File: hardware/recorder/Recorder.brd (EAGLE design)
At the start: 66.5 x 73.7 mm, 23 parts, among them U1 PDM1-S5-D12-S, U2 LM6132BIN, U3 Value, U4 L7908CV, U5 L7808ABV, U6 ZVN4424A, U7 TEENSY_3.6_DIL

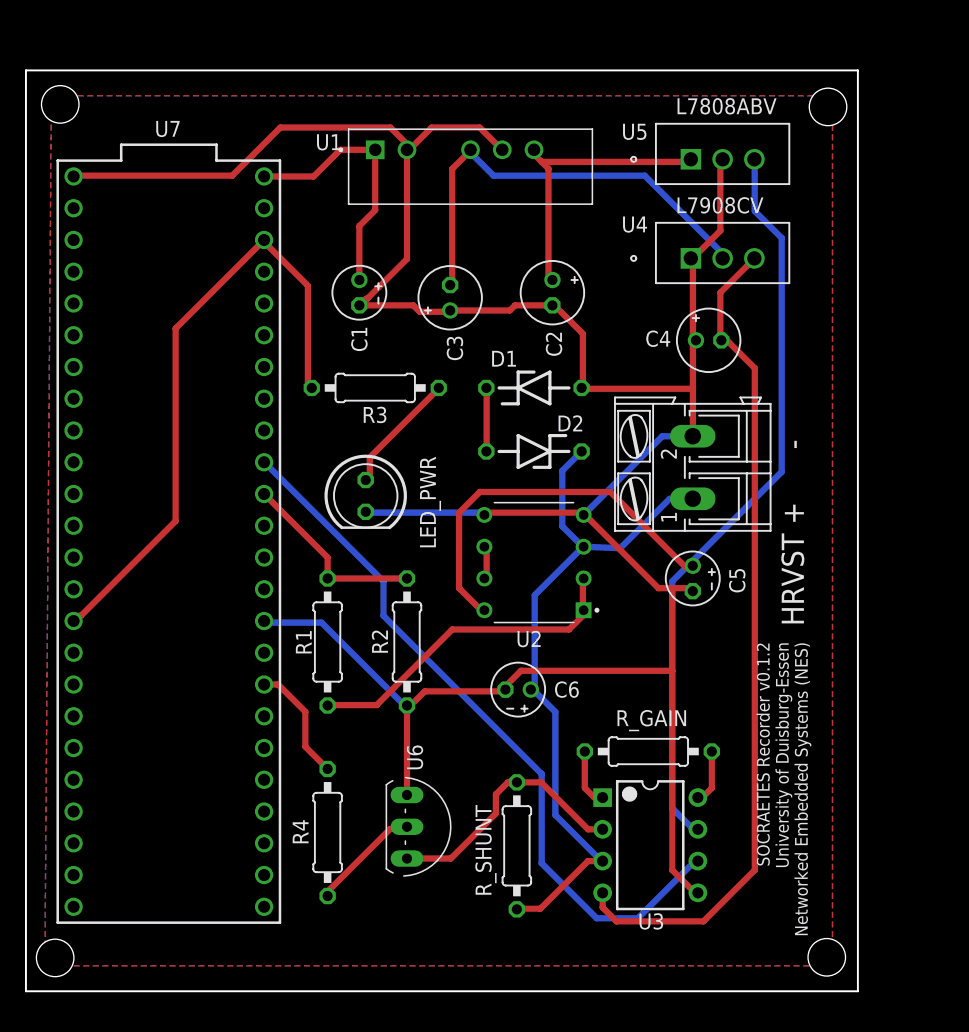
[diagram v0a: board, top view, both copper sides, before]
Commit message: Add vias, fix ground pour on the top layer
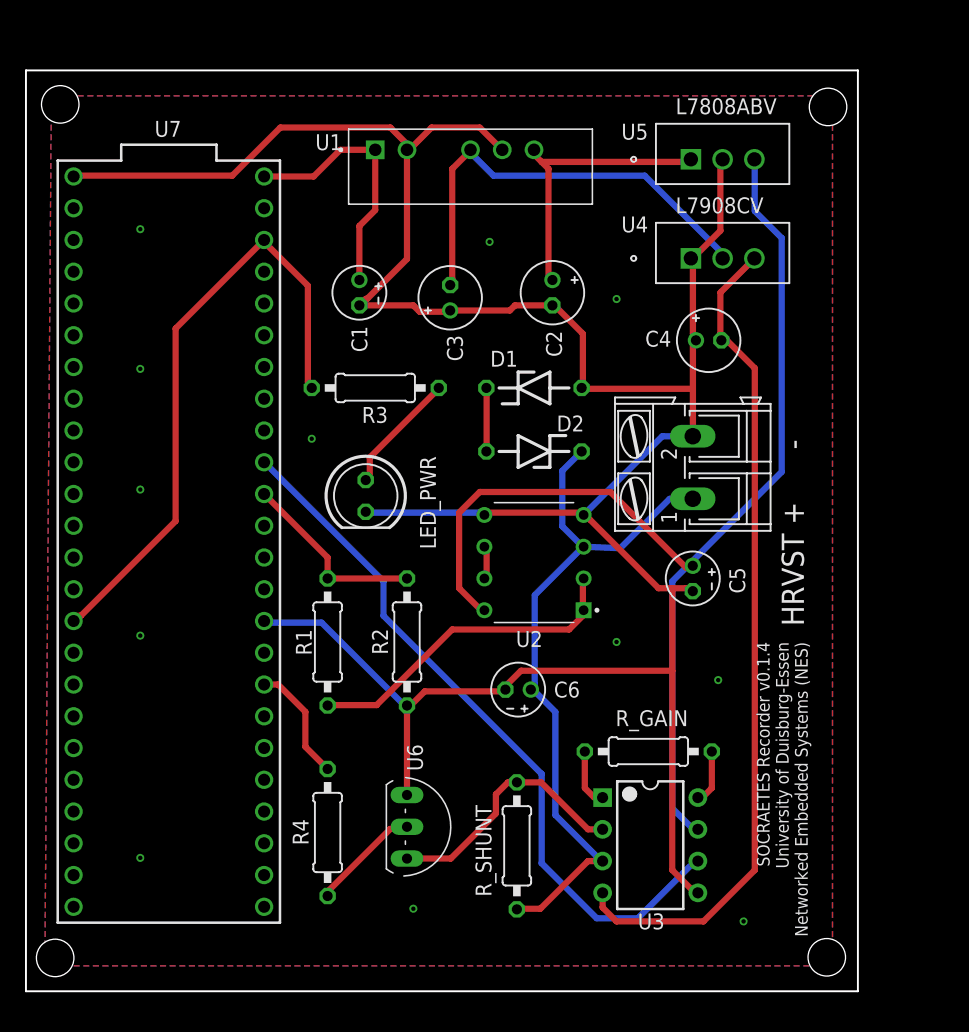
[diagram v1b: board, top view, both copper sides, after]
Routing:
- net GND: vias 0 -> 12
- added copper zone on layer 1, net GND
- removed copper zone on layer 1, net GND1
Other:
- board text added: "SOCRAETES Recorder v0.1.4 University of Duisburg-Essen Networked Embedded Systems (NES)"
- board text removed: "SOCRAETES Recorder v0.1.2 University of Duisburg-Essen Networked Embedded Systems (NES)"
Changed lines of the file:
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@@
 <plain>
 <text x="62.23" y="29.21" size="1.778" layer="25" rot="R90">HRVST +      -</text>
-<text x="58.4708" y="27.94" size="1.016" layer="25" rot="R270">SOCRAETES Recorder v0.1.2
+<text x="58.4708" y="27.94" size="1.016" layer="25" rot="R270">SOCRAETES Recorder v0.1.4
 University of Duisburg-Essen
 Networked Embedded Systems (NES)</text>
@@
 <vertex x="2.032" y="71.628"/>
 </polygon>
+<polygon width="0.5" layer="1" isolate="0.254">
+<vertex x="1.512628125" y="2.032"/>
+<vertex x="64.516" y="2.032"/>
+<vertex x="64.516" y="71.628"/>
+<vertex x="2.032" y="71.628"/>
+</polygon>
+<via x="55.372" y="24.892" extent="1-16" drill="0.35"/>
+<via x="9.144" y="60.96" extent="1-16" drill="0.35"/>
+<via x="9.144" y="49.784" extent="1-16" drill="0.35"/>
+<via x="9.144" y="40.132" extent="1-16" drill="0.35"/>
+<via x="9.144" y="28.448" extent="1-16" drill="0.35"/>
+<via x="9.144" y="10.668" extent="1-16" drill="0.35"/>
+<via x="30.988" y="6.604" extent="1-16" drill="0.35"/>
+<via x="47.244" y="27.94" extent="1-16" drill="0.35"/>
+<via x="57.404" y="5.588" extent="1-16" drill="0.35"/>
+<via x="47.244" y="55.372" extent="1-16" drill="0.35"/>
+<via x="37.084" y="59.944" extent="1-16" drill="0.35"/>
+<via x="22.86" y="44.196" extent="1-16" drill="0.35"/>
 </signal>
 <signal name="+12V">
@@
 <wire x1="30.25" y1="12.99" x2="30.48" y2="13.1572" width="0.5" layer="1"/>
 </signal>
-<signal name="GND1">
-<polygon width="0.5" layer="1" isolate="0.254">
-<vertex x="1.512628125" y="2.032"/>
-<vertex x="64.516" y="2.032"/>
-<vertex x="64.516" y="71.628"/>
-<vertex x="2.032" y="71.628"/>
-</polygon>
-</signal>
 </signals>

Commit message: Migrate recorder board to Teensy 4.1
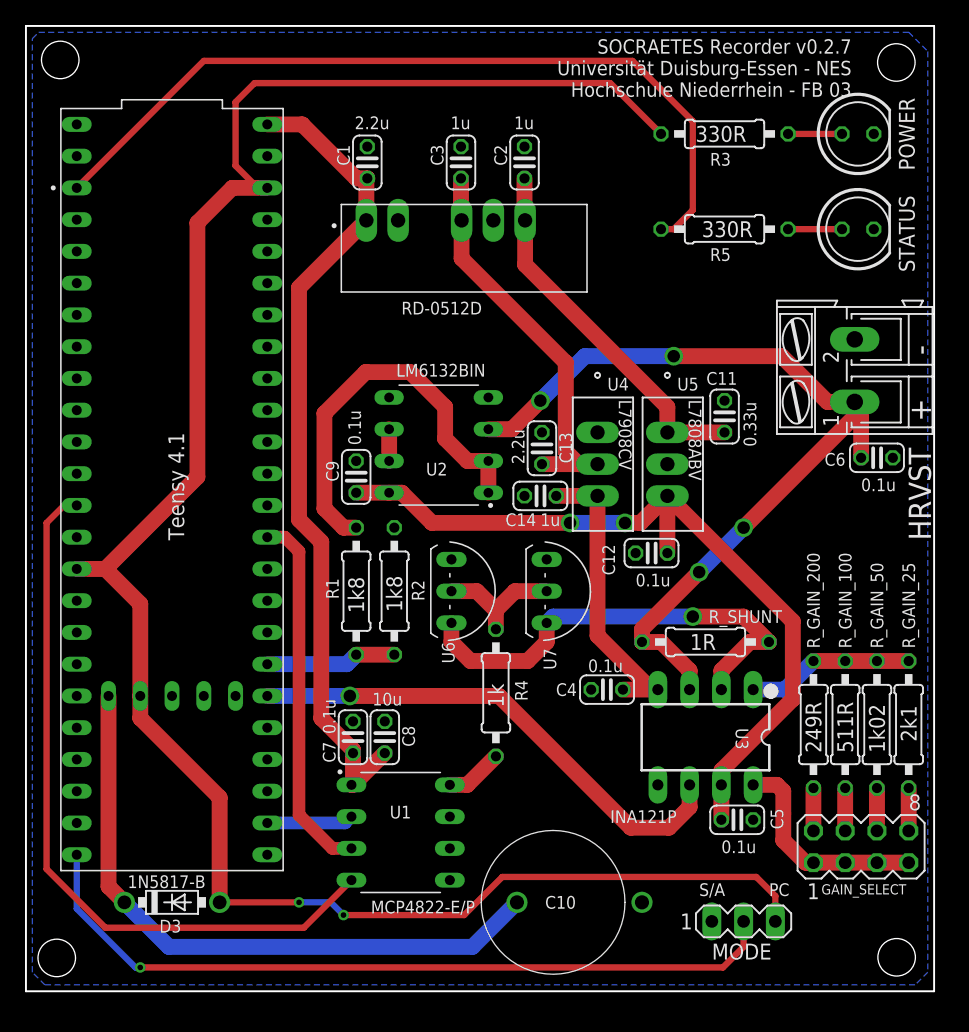
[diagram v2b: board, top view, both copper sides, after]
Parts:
- removed D1, D2: 3v3, diode:ZDIO-7.5
- removed LED_PWR: (no value), led:LED5MM
- removed R_GAIN: (no value), rcl:0207/10
- added C10: EDS224Z3R6H, SamacSys_Parts:EDS224Z3R6H
- added C11: 0.33u, rcl:C025-024X044
- added C12, C7, C9: 0.1u, rcl:C025-024X044
- added C13: 2.2u, rcl:C025-024X044
- added C14: 1u, rcl:C025-024X044
- added C8: 10u, rcl:C025-024X044
- added D3: 1N5817-B, diode:DO41-7.6
- added GAIN_SELECT: (no value), con-lstb:MA04-2
- added MODE: (no value), con-lstb:MA03-1
- added POWER, STATUS: (no value), led:LED5MM
- added PS1: RD-0512D, RD-0512D:CONV_RD-0512D
- added R5: 330R, rcl:0207/10
- added R_GAIN_100: 511R, rcl:0207/10
- added R_GAIN_200: 249R, rcl:0207/10
- added R_GAIN_25: 2k1, rcl:0207/10
- added R_GAIN_50: 1k02, rcl:0207/10
- added U8: DEV-16771_REDUCED_PINS, DEV-16771 (Teensy 41):MODULE_DEV-16771_REDUCED_PINS
- C1, C5, C6: device rcl:E2-4 -> rcl:C025-024X044
- C2, C3: device rcl:E2-5 -> rcl:C025-024X044
- C4: value 1u -> 0.1u; device rcl:E2-5 -> rcl:C025-024X044
- R_SHUNT: value (none) -> 1R
- U1: value PDM1-S5-D12-S -> MCP4822-E/P; device PDM1-S5-D12-S:CONV_PDM1-S5-D12-S -> MCP4822-E_P:DIP787W46P254L927H533Q8
- U7: value TEENSY_3.6_DIL -> ZVN4424A; device Teensy_3_and_LC_Series_Boards_v1.4:TEENSY_3.6_DIL -> NES_Solar_Cell_Recorder_And_Emulator:TO92-CBE
- moved U1 54.6 mm to (30.0, 12.7)
- moved R3 34.5 mm to (55.9, 68.6)
- moved C6 34.2 mm to (68.1, 42.7), turned to 0 degrees
- moved U7 30.7 mm to (41.7, 32.0), turned to 270 degrees
- moved C4 29.1 mm to (46.5, 24.1), turned to 180 degrees
- moved R_SHUNT 22.2 mm to (54.4, 27.9), turned to 0 degrees
- moved U5 21.9 mm to (51.3, 44.7), turned to 270 degrees
- moved C5 19.6 mm to (56.9, 13.7), turned to 0 degrees
- moved U6 19.2 mm to (34.0, 32.0)
- moved R4 17.5 mm to (37.6, 23.9), turned to 270 degrees
- moved U4 15.8 mm to (45.7, 44.7), turned to 270 degrees
- moved HARVESTER_TERMINAL 15.1 mm to (66.3, 49.7)
- moved U2 12.1 mm to (33.0, 43.7)
- moved C3 10.9 mm to (34.8, 66.3)
- moved C2 10.7 mm to (39.9, 66.3), turned to 90 degrees
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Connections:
- removed net AGND: U7.AGND
- removed net MOSFET_DAC: R4.2, U7.A21
- removed net N$4: D1.C, D2.A
- new net +5V: C1.1, C7.1, C8.1, PS1.1, U1.1, U8.VIN
- new net CURRENT_SENSE_AMP_OUTPUT: U3.6, U8.38
- new net DAC_CS: U1.2, U8.34
- new net DAC_MOSI: U1.4, U8.11
- new net DAC_SCK: U1.3, U8.13
- new net HARVESTER_VOLTAGE_DIVIDER_OUTPUT: R1.1, R2.2, U8.39
- new net JUMPER_SELECT_MODE: MODE.2, U8.32
- new net MOSFET_DAC_OUTPUT: R4.2, U1.8
- new net N$12: R_GAIN_100.2, R_GAIN_200.2, R_GAIN_25.2, R_GAIN_50.2, U3.1
- new net N$13: GAIN_SELECT.1, GAIN_SELECT.3, GAIN_SELECT.5, GAIN_SELECT.7, U3.8
- new net N$14: GAIN_SELECT.2, R_GAIN_200.1
- new net STATUS_LED: R5.2, U8.1
- net +12V: now also C11.1, C2.1, PS1.6; no longer C2.+, U1.6
- net +3V3: now also D3.A, MODE.3, U8.3.3V_1, U8.3.3V_2, U8.3.3V_3; no longer U7.3.3V, U7.3.3V3
- net +8V: now also C12.2, C5.1, C9.1; no longer C5.+
- net -12V: now also C13.2, C3.1, PS1.4; no longer C3.-, U1.4
- net -8V: now also C14.2, C4.1; no longer C4.-
- net GND: now also C1.2, C10.2, C11.2, C12.1, C13.1, C14.1, C2.2, C3.2, C4.2, C5.2, C6.2, C7.2, C8.2, C9.2, MODE.1, POWER.K, PS1.2, PS1.5, STATUS.K, U1.7, U7.SOURCE, U8.GND1, U8.GND2, U8.GND3, U8.GND4; no longer C1.-, C2.-, C3.+, C4.+, C5.-, C6.-, D1.A, LED_PWR.K, U1.2, U7.GND, U7.GND1
- net HARVESTER+: now also C6.1; no longer C6.+, D2.C
- net N$1: now also GAIN_SELECT.8, R_GAIN_25.1; no longer R_GAIN.2, U3.1
- net N$10: now also GAIN_SELECT.4, R_GAIN_100.1; no longer U3.6, U7.17/A3
- net N$11: now also U7.GATE
- net N$2: now also C10.1, D3.C, U8.VBAT; no longer C1.+, U1.1, U7.VIN
- net N$3: now also GAIN_SELECT.6, R_GAIN_50.1; no longer R_GAIN.1, U3.8
- net N$6: now also U7.DRAIN
- net N$7: now also R5.1, STATUS.A; no longer R1.1, R2.2, U7.16/A2
- net N$9: now also POWER.A; no longer LED_PWR.A
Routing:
- net GND: track 218.1 -> 0.00 mm, vias 12 -> 0
- net +3V3: track 50.4 -> 163.7 mm, vias 0 -> 2
- net +5V: track 0.00 -> 66.1 mm
- net STATUS_LED: track 0.00 -> 65.8 mm
- net JUMPER_SELECT_MODE: track 0.00 -> 62.3 mm, vias 0 -> 1
- net DAC_MOSI: track 0.00 -> 58.6 mm
- net N$10: track 57.5 -> 3.43 mm
- net -8V: track 66.9 -> 23.9 mm
- net CURRENT_SENSE_AMP_OUTPUT: track 0.00 -> 40.6 mm, vias 0 -> 1
- net N$2: track 20.7 -> 51.4 mm
- net DAC_SCK: track 0.00 -> 29.4 mm
- net +8V: track 90.0 -> 63.8 mm, vias 0 -> 2
- net N$13: track 0.00 -> 17.3 mm
- net N$6: track 20.6 -> 37.0 mm, vias 0 -> 1
- net N$12: track 0.00 -> 13.4 mm
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- removed copper zone on layer 1, net GND
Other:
- board size 66.5 x 73.7 mm -> 72.6 x 77.2 mm
- board text added: "INA121P"
- board text added: "Maximum solar cell current with R_shunt = 2R: GAIN_ia = 25: I_max_record = 66 mA GAIN_ia = 50: I_max_record = 33 mA GAIN_ia = 100: I_max_record = 16.5 mA GAIN_ia = 200: I_max_record = 8.25 mA"
- board text added: "PC"
- board text added: "S/A"
- board text added: "SOCRAETES Recorder v0.2.7 Universität Duisburg-Essen - NES Hochschule Niederrhein - FB 03"
- board text removed: "SOCRAETES Recorder v0.1.4 University of Duisburg-Essen Networked Embedded Systems (NES)"

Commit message: Add error LED to the board
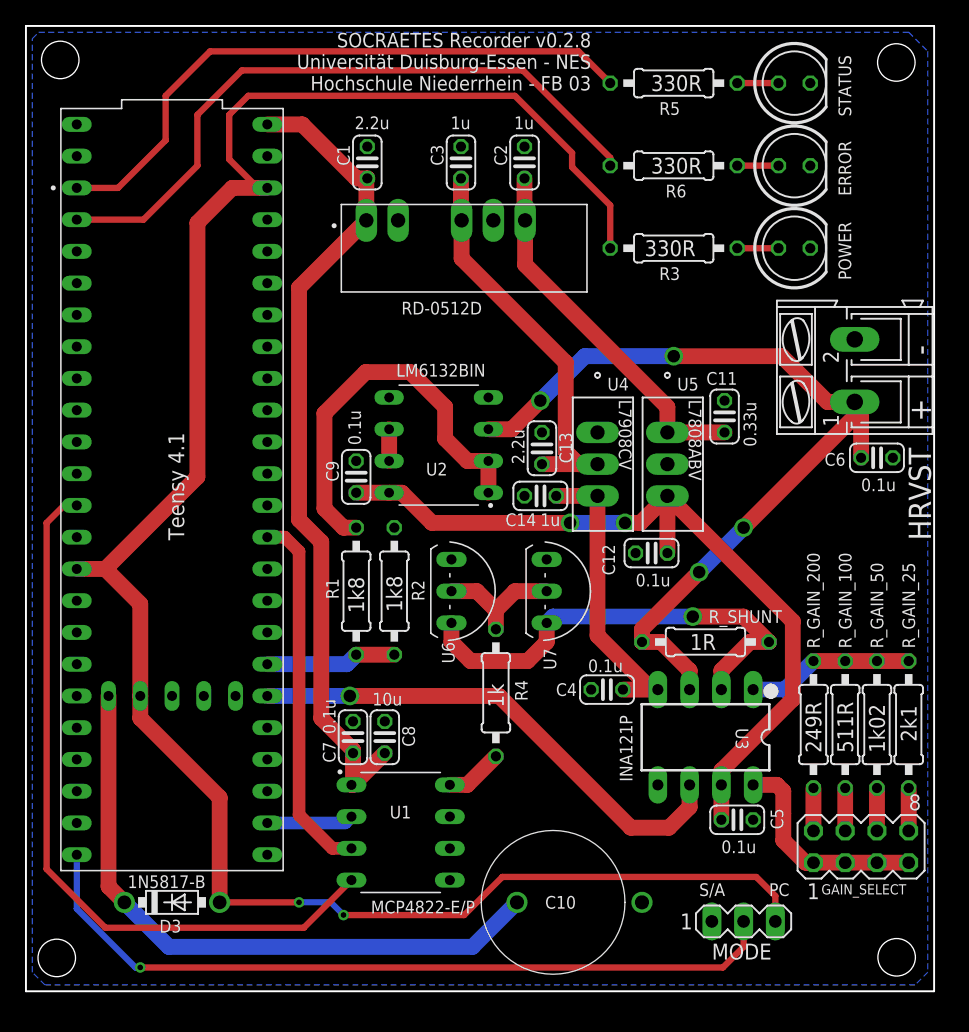
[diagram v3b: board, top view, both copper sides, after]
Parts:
- added ERROR: (no value), led:LED5MM
- added R6: 330R, rcl:0207/10
- moved STATUS 12.7 mm to (61.5, 72.6)
- moved R5 12.4 mm to (51.8, 72.6)
- moved POWER 10.5 mm to (61.5, 59.4)
- moved R3 10.0 mm to (51.8, 59.4)
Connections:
- new net ERROR_LED: R6.2, U8.2
- new net N$4: ERROR.A, R6.1
- net GND: now also ERROR.K
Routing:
- net ERROR_LED: track 0.00 -> 53.5 mm
- net STATUS_LED: track 65.8 -> 50.3 mm
- net N$4: track 0.00 -> 3.30 mm
- net +3V3: track 163.7 -> 165.4 mm
- net N$9: track 4.32 -> 3.30 mm
- net N$7: track 4.32 -> 3.30 mm
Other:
- board text added: "SOCRAETES Recorder v0.2.8 Universität Duisburg-Essen - NES Hochschule Niederrhein - FB 03"
- board text removed: "SOCRAETES Recorder v0.2.7 Universität Duisburg-Essen - NES Hochschule Niederrhein - FB 03"
